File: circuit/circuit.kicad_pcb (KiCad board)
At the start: 2 copper layers, 165.5 x 103 mm, 125 parts, among them J201 Barrel_Jack, J301 Pedal5_In, J302 Guitar_In, J303 Pedal6_In, J304 Amp_Out, J305 Pedal1_In, J306 Pedal7_In, J307 Pedal2_In, J308 Pedal8_In, J309 Pedal3_In, J310 Pedal4_In, SW101 SW_Push, SW102 SW_Push, SW103 SW_Push, SW104 SW_Push, SW105 SW_Push, SW106 SW_Push, SW107 SW_Push, SW108 SW_Push, SW109 SW_Push, SW110 SW_Push, U1 AMS1117-3.3, U10 74HC595, U101 ADG419BN, U11 TL072, U12 TL072, U13 TL072, U14 TL072, U15 TL072, U16 CD4051B, U17 CD4051B, U18 CD4051B, U19 CD4051B, U2 LM7805_TO220, U20 CD4051B, U22 CD4051B, U23 CD4051B, U24 CD4051B, U25 CD4051B, U26 CD4051B, U3 TMA-1215D, U4 LM7905_TO220, U5 ESP32-S3-DevKitC, U7 74HC595, U8 74HC595, U9 74HC595

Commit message: Created pdf and made minor readabilty changes.
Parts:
- added C201: 10uF, Capacitor_THT:C_Axial_L3.8mm_D2.6mm_P7.50mm_Horizontal, F.Cu at (132.0, 46.0)
- added C202: 100uF, Capacitor_THT:C_Axial_L3.8mm_D2.6mm_P7.50mm_Horizontal, F.Cu at (132.0, 51.0)
- added C203: 0.1uF, Capacitor_THT:C_Axial_L3.8mm_D2.6mm_P7.50mm_Horizontal, F.Cu at (65.0, 30.0)
- added C204: 0.1uF, Capacitor_THT:C_Axial_L3.8mm_D2.6mm_P7.50mm_Horizontal, F.Cu at (107.0, 66.0)
- C101, C102, C103, C104, C105, C106, C107, C108, C109, C110: value 0.1mF -> .1uF
- C111, C112, C113, C114, C115, C116, C117, C118, C119, C120, C121, C122, C123, C124, C125, C126, C127, C128, C129, C130, C131, C132, C206, C208: value 0.1mF -> 0.1uF
- C205, C207: value 0.33mF -> 0.33uF
- C209, C210: value 10mF -> 10uF
- C303, C304, C305, C306, C311, C312, C313, C314, C318, C319: value 1mF -> 1uF
- moved C313 100.2 mm to (133.0, 96.0)
- moved C201 94.2 mm to (196.0, 79.5), turned to 180 degrees
- moved NT101 89.1 mm to (187.0, 117.0)
- moved C304 84.3 mm to (152.0, 117.0)
- moved R306 82.7 mm to (125.0, 94.0)
- moved U2 82.5 mm to (139.5, 121.5), turned to 180 degrees
- moved C318 82.0 mm to (121.0, 85.0)
- moved C205 80.3 mm to (137.0, 112.0)
- moved C206 76.7 mm to (143.0, 117.0), turned to 180 degrees
- moved SW110 75.2 mm to (180.0, 102.0), turned to 180 degrees
- moved C309 73.8 mm to (125.0, 60.0)
- moved C109 73.2 mm to (174.3, 96.0)
- moved U3 73.0 mm to (140.0, 57.0)
- moved R308 72.8 mm to (117.0, 70.0)
- moved C303 70.2 mm to (119.0, 90.0)
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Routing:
- net VIN_12V: track 155.3 -> 8.70 mm
- net Net-(Disp101-SDA): track 107.1 -> 28.5 mm
- net Net-(Disp101-SCL): track 105.8 -> 27.5 mm
- net 3.3V: track 70.4 -> 0.00 mm, vias 1 -> 0
- net Net-(U5-GPIO9/ADC1_CH8): track 5.15 -> 71.6 mm, vias 0 -> 2
- net Net-(D201-A): track 68.8 -> 15.1 mm
- net Net-(U5-GPIO8/ADC1_CH7): track 4.89 -> 56.7 mm
- net Net-(U5-GPIO7/ADC1_CH6): track 5.23 -> 57.0 mm
- net Net-(U5-GPIO14/ADC2_CH3): track 89.1 -> 41.0 mm
- net Net-(U1-VO): track 53.6 -> 6.30 mm
- net PEDAL_5_IN: track 45.0 -> 0.00 mm
- net /U9_Q4: track 44.1 -> 0.00 mm
- net /U9_Q6: track 43.5 -> 0.00 mm
- net /U9_Q5: track 43.5 -> 0.00 mm
- net SR_STCP: track 0.00 -> 41.7 mm
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
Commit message: Changed default pin assignments and setp sdkconfig.defaults
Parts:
- moved C113 165.6 mm to (-2.25, 108.5)
- moved C319 151.1 mm to (-16.1, 85.3)
- moved R308 140.6 mm to (-11.6, 13.2)
- moved R301 138.8 mm to (-9.12, 90.3)
- moved C318 133.9 mm to (7.38, 14.2)
- moved U10 131.9 mm to (119.5, -67.1)
- moved C313 128.5 mm to (4.88, 106.3)
- moved U18 126.2 mm to (-13.6, 22.2)
- moved C210 122.3 mm to (10.9, 111.3)
- moved R302 122.0 mm to (11.8, 94.5)
- moved R306 119.4 mm to (5.88, 102.3)
- moved C118 117.4 mm to (135.2, 9.00)
- moved C303 117.2 mm to (1.88, 94.3)
- moved U17 115.7 mm to (135.1, 15.4)
- moved C129 115.0 mm to (163.0, 120.0)
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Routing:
- net SR_OE: track 0.00 -> 216.6 mm
- net -15V: track 0.00 -> 87.2 mm
- net SR_STCP: track 41.7 -> 118.6 mm, vias 0 -> 1
- net +15V: track 0.00 -> 74.6 mm
- net Net-(U12-1+): track 0.00 -> 63.1 mm
- net SR_SHCP: track 36.1 -> 80.9 mm, vias 0 -> 1
- net SR_DS: track 32.3 -> 74.5 mm, vias 0 -> 3
- net /IO Routing/U7_Q5: track 0.00 -> 37.3 mm
- net /IO Routing/U7_Q6: track 0.00 -> 35.5 mm
- net /IO Routing/U7_Q4: track 0.00 -> 35.3 mm
- net /IO Routing/U7_Q7: track 0.00 -> 33.7 mm
- net /IO Routing/U7_Q3: track 0.00 -> 20.6 mm
- net /IO Routing/U7_Q2: track 0.00 -> 20.6 mm
- net /IO Routing/U7_Q0: track 0.00 -> 14.3 mm
- net 3.3V: track 0.00 -> 2.54 mm
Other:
- board size 165.5 x 103 mm -> 165.5 x 142.5 mm

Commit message: Very tentative PCB layout, Code compiles but needs major functionality testing.
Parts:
- removed the C201 at (196.0, 79.5)
- removed the C201 at (132.0, 45.0)
- removed the C202 at (188.8, 83.0)
- removed the C202 at (132.0, 50.0)
- removed the C203 at (52.0, 50.0)
- removed the C203 at (52.0, 45.0)
- removed the C204 at (109.0, 51.0)
- removed the C204 at (49.0, 30.0)
- added C201: 10uF, Capacitor_THT:C_Axial_L3.8mm_D2.6mm_P7.50mm_Horizontal, F.Cu at (184.5, 136.5)
- added C202: 100uF, Capacitor_THT:C_Axial_L3.8mm_D2.6mm_P7.50mm_Horizontal, F.Cu at (195.0, 137.5)
- added C203: 0.1uF, Capacitor_THT:C_Axial_L3.8mm_D2.6mm_P7.50mm_Horizontal, F.Cu at (117.0, 91.0)
- added C204: 0.1uF, Capacitor_THT:C_Axial_L3.8mm_D2.6mm_P7.50mm_Horizontal, F.Cu at (135.2, 126.5)
- added C801: 0.1uF, Capacitor_THT:C_Axial_L3.8mm_D2.6mm_P7.50mm_Horizontal, F.Cu at (170.8, 78.9)
- added C802: 0.1uF, Capacitor_THT:C_Axial_L3.8mm_D2.6mm_P7.50mm_Horizontal, F.Cu at (181.3, 79.9)
- added D100: LED_PWR, Connector_Wire:SolderWire-0.1sqmm_1x02_P3.6mm_D0.4mm_OD1mm, F.Cu at (234.9, 149.8)
- added D801: Pedal_1, Connector_Wire:SolderWire-0.1sqmm_1x02_P3.6mm_D0.4mm_OD1mm, F.Cu at (150.5, 38.8)
- added D802: Pedal_2, Connector_Wire:SolderWire-0.1sqmm_1x02_P3.6mm_D0.4mm_OD1mm, F.Cu at (156.0, 38.8)
- added D803: Pedal_3, Connector_Wire:SolderWire-0.1sqmm_1x02_P3.6mm_D0.4mm_OD1mm, F.Cu at (161.5, 38.8)
- added D804: Pedal_4, Connector_Wire:SolderWire-0.1sqmm_1x02_P3.6mm_D0.4mm_OD1mm, F.Cu at (167.0, 38.8)
- added D805: Status, Connector_Wire:SolderWire-0.1sqmm_1x02_P3.6mm_D0.4mm_OD1mm, F.Cu at (172.5, 38.5)
- added D806: Pedal_5, Connector_Wire:SolderWire-0.1sqmm_1x02_P3.6mm_D0.4mm_OD1mm, F.Cu at (178.0, 38.5)
- added D807: Pedal_6, Connector_Wire:SolderWire-0.1sqmm_1x02_P3.6mm_D0.4mm_OD1mm, F.Cu at (183.5, 38.5)
- added D808: Pedal_7, Connector_Wire:SolderWire-0.1sqmm_1x02_P3.6mm_D0.4mm_OD1mm, F.Cu at (189.0, 38.3)
- added D809: Pedal_8, Connector_Wire:SolderWire-0.1sqmm_1x02_P3.6mm_D0.4mm_OD1mm, F.Cu at (194.5, 38.3)
- added R101: 100, Resistor_THT:R_Axial_DIN0204_L3.6mm_D1.6mm_P5.08mm_Horizontal, F.Cu at (229.4, 145.3)
- added R801: 150, Resistor_THT:R_Axial_DIN0204_L3.6mm_D1.6mm_P5.08mm_Horizontal, F.Cu at (147.6, 43.4)
- added R802: 150, Resistor_THT:R_Axial_DIN0204_L3.6mm_D1.6mm_P5.08mm_Horizontal, F.Cu at (153.8, 46.2)
- added R803: 150, Resistor_THT:R_Axial_DIN0204_L3.6mm_D1.6mm_P5.08mm_Horizontal, F.Cu at (160.1, 43.4)
- added R804: 150, Resistor_THT:R_Axial_DIN0204_L3.6mm_D1.6mm_P5.08mm_Horizontal, F.Cu at (166.4, 46.2)
- added R805: 150, Resistor_THT:R_Axial_DIN0204_L3.6mm_D1.6mm_P5.08mm_Horizontal, F.Cu at (172.7, 43.4)
- added R806: 150, Resistor_THT:R_Axial_DIN0204_L3.6mm_D1.6mm_P5.08mm_Horizontal, F.Cu at (178.9, 46.2)
- added R807: 150, Resistor_THT:R_Axial_DIN0204_L3.6mm_D1.6mm_P5.08mm_Horizontal, F.Cu at (232.4, 95.8)
- added R808: 150, Resistor_THT:R_Axial_DIN0204_L3.6mm_D1.6mm_P5.08mm_Horizontal, F.Cu at (185.3, 43.4)
- added R809: 150, Resistor_THT:R_Axial_DIN0204_L3.6mm_D1.6mm_P5.08mm_Horizontal, F.Cu at (191.5, 46.2)
- added RV101: 500, Potentiometer_THT:Potentiometer_Bourns_3339P_Vertical, F.Cu at (223.5, 147.8)
- added U801: 74HC595, Package_DIP:CERDIP-16_W7.62mm_SideBrazed, F.Cu at (163.4, 55.1)
- added U802: 74HC595, Package_DIP:CERDIP-16_W7.62mm_SideBrazed, F.Cu at (173.7, 56.1)
- C101, C102, C103, C104, C105, C106, C107, C108, C109, C110, C701, C702, C703, C704: value .1uF -> 0.1uF
- Disp101: footprint Connector_JST:JST_EH_B4B-EH-A_1x04_P2.50mm_Vertical -> Connector_PinHeader_1.00mm:PinHeader_1x04_P1.00mm_Vertical
- J301, J302, J303, J304, J305, J306, J307, J308, J309, J310: footprint Connector_Wire:SolderWire-0.1sqmm_1x02_P3.6mm_D0.4mm_OD1mm -> Bay:Pedal_Jack
- SW101: value SW_Push -> Pedal_1
- SW102: value SW_Push -> Pedal_2
- SW103: value SW_Push -> Pedal_3
- SW104: value SW_Push -> Pedal_4
- SW105: value SW_Push -> Pedal_5
- SW106: value SW_Push -> Pedal_6
- SW107: value SW_Push -> Pedal_7
- SW108: value SW_Push -> Pedal_8
- SW109: value SW_Push -> Program
- SW110: value SW_Push -> Preset
- moved C318 254.6 mm to (229.4, 138.8)
- moved R309 240.0 mm to (203.4, 123.8)
- moved C319 224.8 mm to (203.4, 133.8)
- moved C303 220.4 mm to (218.4, 135.8)
- moved C210 217.5 mm to (226.4, 140.8)
- moved R304 213.9 mm to (222.4, 92.8)
- moved C311 212.7 mm to (221.4, 96.8)
- moved R308 199.3 mm to (153.4, 125.0)
- moved C313 171.4 mm to (175.4, 123.8)
- moved R302 171.3 mm to (179.4, 129.8)
- moved R301 158.4 mm to (145.0, 127.0)
- moved R306 149.7 mm to (155.0, 89.0)
- moved C127 144.3 mm to (140.0, 79.3), turned to 180 degrees
- moved C131 138.3 mm to (129.7, 79.2), turned to 180 degrees
- moved C126 133.4 mm to (142.8, 49.1)
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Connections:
- net /Pedal Routing 1 - 4/U8_Q0 renamed /Matrix Shift Registers/U8_Q0
- net /Pedal Routing 1 - 4/U8_Q1 renamed /Matrix Shift Registers/U8_Q1
- net /Pedal Routing 1 - 4/U8_Q2 renamed /Matrix Shift Registers/U8_Q2
- net /Pedal Routing 1 - 4/U8_Q3 renamed /Matrix Shift Registers/U8_Q3
- net /Pedal Routing 1 - 4/U8_Q4 renamed /Matrix Shift Registers/U8_Q4
- net /Pedal Routing 1 - 4/U8_Q5 renamed /Matrix Shift Registers/U8_Q5
- net /Pedal Routing 1 - 4/U8_Q6 renamed /Matrix Shift Registers/U8_Q6
- net /Pedal Routing 1 - 4/U8_Q7 renamed /Matrix Shift Registers/U8_Q7
- net SR_DS renamed MATRIX_SR_DS
- U5 pad 27: unconnected-(U5-GPIO21-Pad27) -> LED_SR_DS
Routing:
- net AGND: track 0.00 -> 761.7 mm
- net GND: track 0.00 -> 618.4 mm, vias 0 -> 3
- net 3.3V: track 2.54 -> 424.9 mm, vias 0 -> 1
- net +5V: track 3.88 -> 352.8 mm, vias 0 -> 1
- net -5V: track 0.00 -> 294.6 mm
- net ROW_6: track 0.00 -> 206.8 mm, vias 0 -> 2
- net ROW_1: track 0.00 -> 184.6 mm, vias 0 -> 5
- net ROW_3: track 0.00 -> 174.4 mm, vias 0 -> 2
- net ROW_4: track 0.00 -> 166.4 mm, vias 0 -> 2
- net ROW_5: track 0.00 -> 161.1 mm
- net ROW_2: track 0.00 -> 158.2 mm
- net ROW_7: track 0.00 -> 157.1 mm
- net Net-(C314-Pad1): track 0.00 -> 137.3 mm
- net SR_SHCP: track 80.9 -> 216.2 mm, vias 1 -> 5
- net ROW_9: track 0.00 -> 133.7 mm, vias 0 -> 1
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- removed copper zone on B.Cu, net AGND
- removed copper zone on B.Cu, net GND
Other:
- board size 165.5 x 142.5 mm -> 183.2 x 119.6 mm

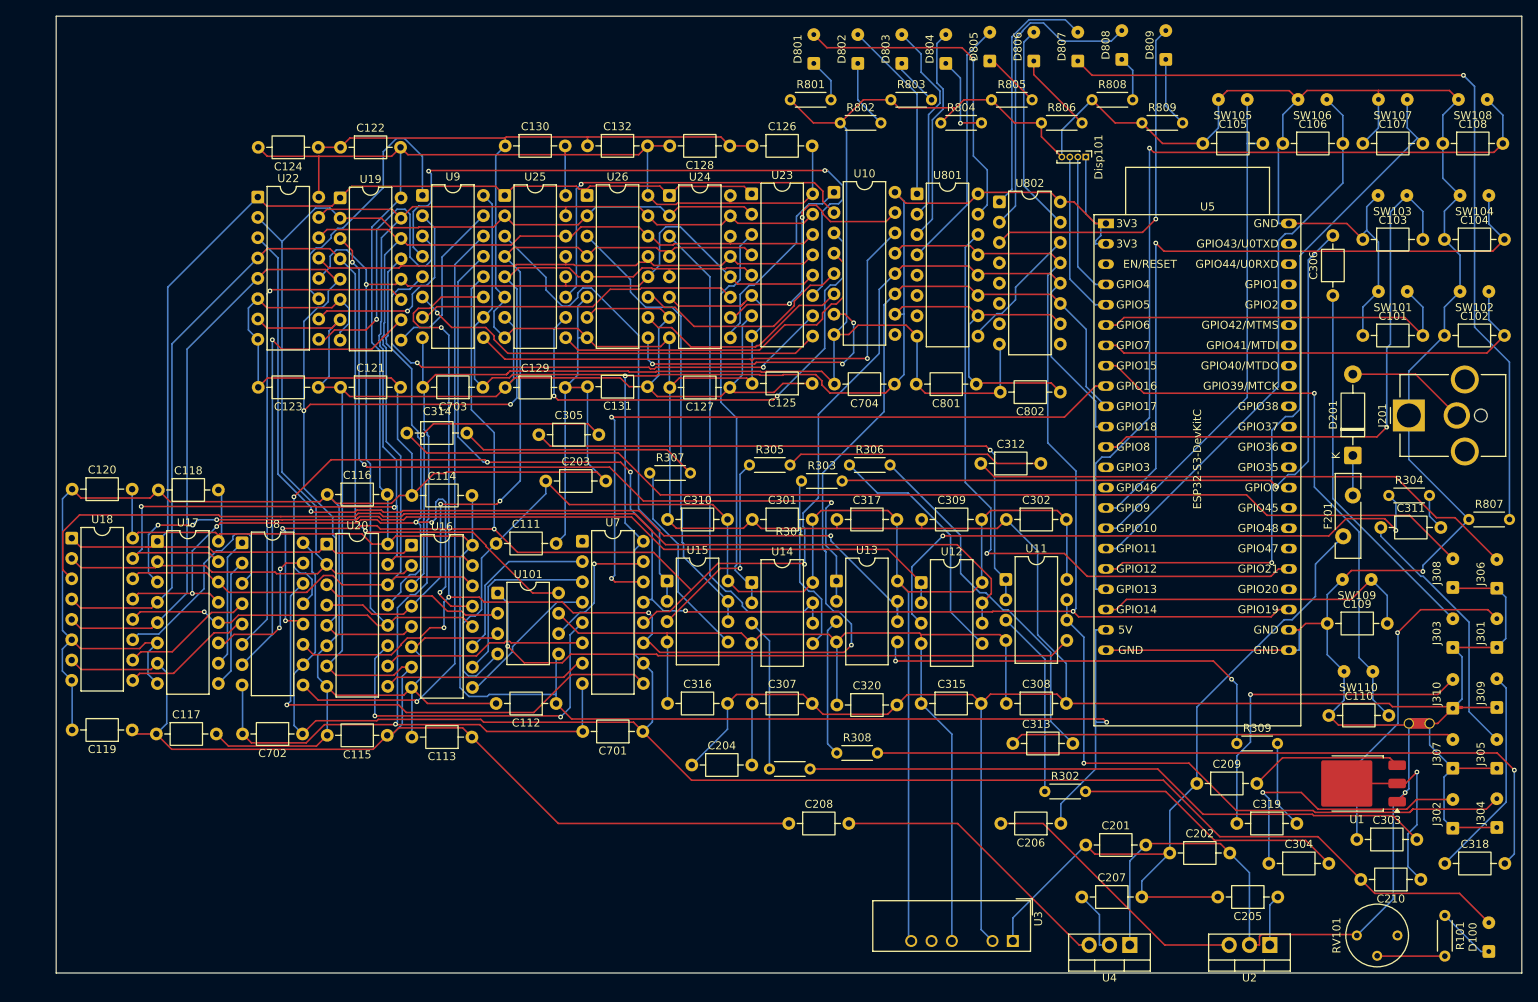
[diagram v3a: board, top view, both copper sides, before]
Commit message: Re-annotation of circuit, new PCB routing, updated PDF
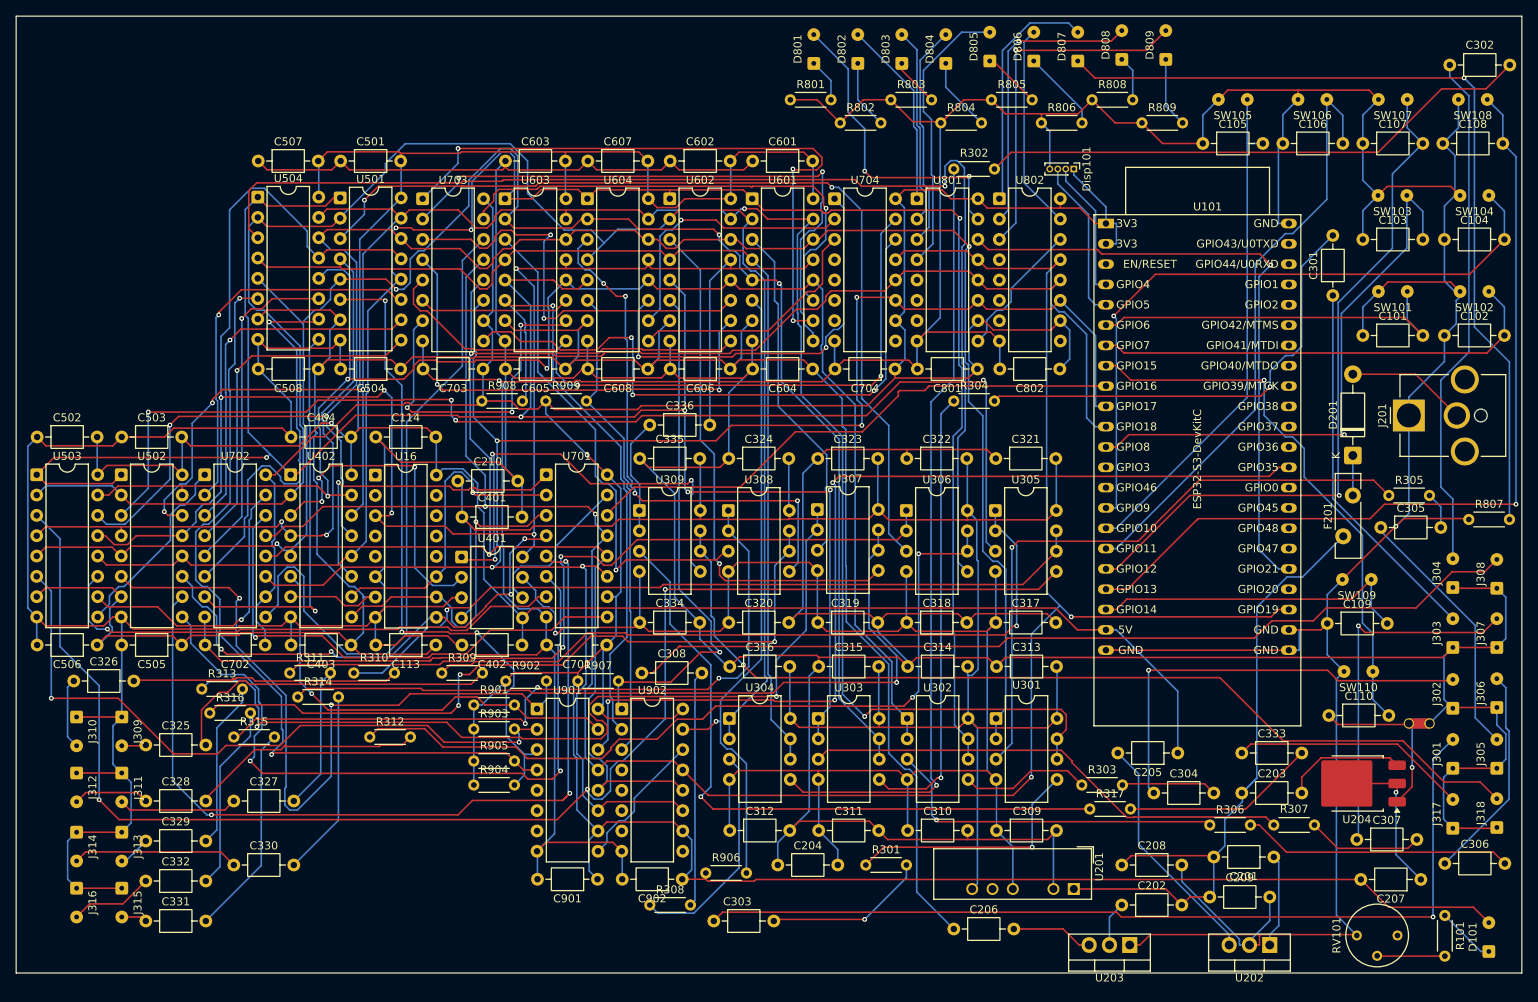
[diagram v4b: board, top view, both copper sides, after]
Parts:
- added C317: 0.1uF, Capacitor_THT:C_Axial_L3.8mm_D2.6mm_P7.50mm_Horizontal, F.Cu at (173.2, 108.7)
- added C318: 0.1uF, Capacitor_THT:C_Axial_L3.8mm_D2.6mm_P7.50mm_Horizontal, F.Cu at (162.1, 108.7)
- added C319: 0.1uF, Capacitor_THT:C_Axial_L3.8mm_D2.6mm_P7.50mm_Horizontal, F.Cu at (151.0, 108.7)
- added C320: 0.1uF, Capacitor_THT:C_Axial_L3.8mm_D2.6mm_P7.50mm_Horizontal, F.Cu at (139.9, 108.7)
- added C321: 0.1uF, Capacitor_THT:C_Axial_L3.8mm_D2.6mm_P7.50mm_Horizontal, F.Cu at (173.2, 88.2)
- added C322: 0.1uF, Capacitor_THT:C_Axial_L3.8mm_D2.6mm_P7.50mm_Horizontal, F.Cu at (162.1, 88.2)
- added C323: 0.1uF, Capacitor_THT:C_Axial_L3.8mm_D2.6mm_P7.50mm_Horizontal, F.Cu at (151.0, 88.2)
- added C324: 0.1uF, Capacitor_THT:C_Axial_L3.8mm_D2.6mm_P7.50mm_Horizontal, F.Cu at (139.9, 88.2)
- added C325: 1uF, Capacitor_THT:C_Axial_L3.8mm_D2.6mm_P7.50mm_Horizontal, F.Cu at (67.0, 124.0)
- added C326: 1uF, Capacitor_THT:C_Axial_L3.8mm_D2.6mm_P7.50mm_Horizontal, F.Cu at (58.0, 116.0)
- added C327: 1uF, Capacitor_THT:C_Axial_L3.8mm_D2.6mm_P7.50mm_Horizontal, F.Cu at (78.0, 131.0)
- added C328: 1uF, Capacitor_THT:C_Axial_L3.8mm_D2.6mm_P7.50mm_Horizontal, F.Cu at (67.0, 131.0)
- added C329: 1uF, Capacitor_THT:C_Axial_L3.8mm_D2.6mm_P7.50mm_Horizontal, F.Cu at (67.0, 136.0)
- added C330: 1uF, Capacitor_THT:C_Axial_L3.8mm_D2.6mm_P7.50mm_Horizontal, F.Cu at (78.0, 139.0)
- added C331: 1uF, Capacitor_THT:C_Axial_L3.8mm_D2.6mm_P7.50mm_Horizontal, F.Cu at (67.0, 146.0)
- added C332: 1uF, Capacitor_THT:C_Axial_L3.8mm_D2.6mm_P7.50mm_Horizontal, F.Cu at (67.0, 141.0)
- added C901: 0.1uF, Capacitor_THT:C_Axial_L3.8mm_D2.6mm_P7.50mm_Horizontal, F.Cu at (123.5, 140.8)
- added C902: 0.1uF, Capacitor_THT:C_Axial_L3.8mm_D2.6mm_P7.50mm_Horizontal, F.Cu at (134.1, 140.8)
- added J309: FX_S_1, Bay:Pedal_Jack, F.Cu at (64.0, 120.5)
- added J310: FX_S_2, Bay:Pedal_Jack, F.Cu at (58.4, 120.5)
- added J311: FX_S_3, Bay:Pedal_Jack, F.Cu at (64.0, 127.5)
- added J312: FX_S_4, Bay:Pedal_Jack, F.Cu at (58.4, 127.5)
- added J313: FX_S_5, Bay:Pedal_Jack, F.Cu at (64.0, 134.9)
- added J314: FX_S_6, Bay:Pedal_Jack, F.Cu at (58.4, 134.9)
- added J315: FX_S_7, Bay:Pedal_Jack, F.Cu at (64.0, 141.9)
- added J316: FX_S_8, Bay:Pedal_Jack, F.Cu at (58.4, 141.9)
- added R309: 10k, Resistor_THT:R_Axial_DIN0204_L3.6mm_D1.6mm_P5.08mm_Horizontal, F.Cu at (104.0, 115.0)
- added R310: 10k, Resistor_THT:R_Axial_DIN0204_L3.6mm_D1.6mm_P5.08mm_Horizontal, F.Cu at (93.0, 115.0)
- added R311: 10k, Resistor_THT:R_Axial_DIN0204_L3.6mm_D1.6mm_P5.08mm_Horizontal, F.Cu at (85.0, 115.0)
- added R312: 10k, Resistor_THT:R_Axial_DIN0204_L3.6mm_D1.6mm_P5.08mm_Horizontal, F.Cu at (95.0, 123.0)
- added R313: 10k, Resistor_THT:R_Axial_DIN0204_L3.6mm_D1.6mm_P5.08mm_Horizontal, F.Cu at (74.0, 117.0)
- added R314: 10k, Resistor_THT:R_Axial_DIN0204_L3.6mm_D1.6mm_P5.08mm_Horizontal, F.Cu at (86.0, 118.0)
- added R315: 10k, Resistor_THT:R_Axial_DIN0204_L3.6mm_D1.6mm_P5.08mm_Horizontal, F.Cu at (78.0, 123.0)
- added R316: 10k, Resistor_THT:R_Axial_DIN0204_L3.6mm_D1.6mm_P5.08mm_Horizontal, F.Cu at (75.0, 120.0)
- added R901: 10k, Resistor_THT:R_Axial_DIN0204_L3.6mm_D1.6mm_P5.08mm_Horizontal, F.Cu at (108.0, 119.0)
- added R902: 10k, Resistor_THT:R_Axial_DIN0204_L3.6mm_D1.6mm_P5.08mm_Horizontal, F.Cu at (112.0, 116.0)
- added R903: 10k, Resistor_THT:R_Axial_DIN0204_L3.6mm_D1.6mm_P5.08mm_Horizontal, F.Cu at (108.0, 122.0)
- added R904: 10k, Resistor_THT:R_Axial_DIN0204_L3.6mm_D1.6mm_P5.08mm_Horizontal, F.Cu at (108.0, 129.0)
- added R905: 10k, Resistor_THT:R_Axial_DIN0204_L3.6mm_D1.6mm_P5.08mm_Horizontal, F.Cu at (108.0, 126.0)
- added R906: 10k, Resistor_THT:R_Axial_DIN0204_L3.6mm_D1.6mm_P5.08mm_Horizontal, F.Cu at (137.0, 140.0)
- added R907: 10k, Resistor_THT:R_Axial_DIN0204_L3.6mm_D1.6mm_P5.08mm_Horizontal, F.Cu at (121.0, 116.0)
- added R908: 10k, Resistor_THT:R_Axial_DIN0204_L3.6mm_D1.6mm_P5.08mm_Horizontal, F.Cu at (109.0, 81.0)
- added R909: 10k, Resistor_THT:R_Axial_DIN0204_L3.6mm_D1.6mm_P5.08mm_Horizontal, F.Cu at (117.0, 81.0)
- added U305: TL072, Package_DIP:CERDIP-8_W7.62mm_SideBrazed, F.Cu at (173.2, 94.7)
- added U306: TL072, Package_DIP:CERDIP-8_W7.62mm_SideBrazed, F.Cu at (162.1, 94.7)
- added U307: TL072, Package_DIP:CERDIP-8_W7.62mm_SideBrazed, F.Cu at (150.9, 94.6)
- added U308: TL072, Package_DIP:CERDIP-8_W7.62mm_SideBrazed, F.Cu at (139.8, 94.7)
- added U901: 74HC595, Package_DIP:CERDIP-16_W7.62mm_SideBrazed, F.Cu at (115.9, 119.5)
- added U902: 74HC595, Package_DIP:CERDIP-16_W7.62mm_SideBrazed, F.Cu at (126.5, 119.5)
- J301: renamed from J307; value Pedal2_In -> FX_R_2
- J302: renamed from J310; value Pedal4_In -> FX_R_4
- J303: value Pedal6_In -> FX_R_56
- J304: renamed from J308; value Pedal8_In -> FX_R_8
- J305: value Pedal1_In -> FX_R_1
- J306: renamed from J309; value Pedal3_In -> FX_R_3
- J307: renamed from J301; value Pedal5_In -> FX_R_5
- J308: renamed from J306; value Pedal7_In -> FX_R_7
- moved C302 138.2 mm to (230.0, 39.0)
- moved R307 63.4 mm to (208.0, 134.0)
- moved R308 56.4 mm to (130.0, 144.0)
- moved R302 53.7 mm to (168.0, 52.0)
- moved R301 50.0 mm to (157.0, 139.0)
- moved C308 49.8 mm to (129.0, 115.0)
- moved R306 47.5 mm to (200.0, 134.0)
- moved C334 46.9 mm to (128.8, 108.7)
- moved U309 46.6 mm to (128.7, 94.7)
- moved C335 46.4 mm to (128.8, 88.2)
- moved C303 43.5 mm to (138.0, 146.0)
- moved C206 24.5 mm to (168.0, 147.0)
- moved R304 21.5 mm to (168.0, 81.0)
- moved C313 20.6 mm to (173.3, 114.2)
- moved C314 20.4 mm to (162.2, 114.2)
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- renumbered C205 to C201, C207 to C202, C209 to C203, C206 to C205, C208 to C206, C210 to C207, C201 to C208, C202 to C209, C203 to C210, C306 to C301, C314 to C302, C313 to C303, C319 to C304, C311 to C305, C318 to C306, C303 to C307, C312 to C308, C315 to C309, C320 to C310, C307 to C311, C316 to C312, C309 to C313, C317 to C314, C301 to C315, C310 to C316, C304 to C333, C308 to C334, C302 to C335, C305 to C336, C111 to C401, C112 to C402, C115 to C403, C116 to C404, C122 to C501, C120 to C502, C118 to C503, C121 to C504, C117 to C505, C119 to C506, C124 to C507, C123 to C508, C126 to C601, C128 to C602, C130 to C603, C125 to C604, C129 to C605, C127 to C606, C132 to C607, C131 to C608, D100 to D101, J302 to J317, J304 to J318, R306 to R301, R307 to R302, R309 to R303, R303 to R304, R304 to R305, R308 to R306, R301 to R307, R305 to R308, R302 to R317, U5 to U101, U3 to U201, U2 to U202, U4 to U203, U1 to U204, U12 to U301, U13 to U302, U14 to U303, U15 to U304, U11 to U309, U101 to U401, U20 to U402, U19 to U501, U17 to U502, U18 to U503, U22 to U504, U23 to U601, U24 to U602, U25 to U603, U26 to U604, U7 to U701, U8 to U702, U9 to U703, U10 to U704
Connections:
- U101 pad 32: unconnected-(U5-GPIO35-Pad32) -> INHIBIT_SR_DS
- U301 pad 1: PEDAL_1_IN -> FX_R_1
- U301 pad 2: PEDAL_1_IN -> FX_R_1
- U301 pad 6: PEDAL_2_IN -> FX_R_2
- U301 pad 7: PEDAL_2_IN -> FX_R_2
- U302 pad 1: PEDAL_3_IN -> FX_R_3
- U302 pad 2: PEDAL_3_IN -> FX_R_3
- U302 pad 6: PEDAL_4_IN -> FX_R_4
- U302 pad 7: PEDAL_4_IN -> FX_R_4
- U303 pad 1: PEDAL_5_IN -> FX_R_5
- U303 pad 2: PEDAL_5_IN -> FX_R_5
- U303 pad 6: PEDAL_6_IN -> FX_R_6
- U303 pad 7: PEDAL_6_IN -> FX_R_6
- U304 pad 1: PEDAL_7_IN -> FX_R_7
- U304 pad 2: PEDAL_7_IN -> FX_R_7
- U304 pad 6: PEDAL_8_IN -> FX_R_8
- U304 pad 7: PEDAL_8_IN -> FX_R_8
- U401 pad 8: ROW_9 -> GUITAR_IN
- U402 pad 1: ROW_5 -> FX_R_5
- U402 pad 10: /IO Routing/U7_Q6 -> /IO Routing/U7_Q2
- U402 pad 11: /IO Routing/U7_Q5 -> /IO Routing/U7_Q1
- U402 pad 12: ROW_4 -> FX_R_4
- U402 pad 13: ROW_1 -> FX_R_1
- U402 pad 14: ROW_2 -> FX_R_2
- U402 pad 15: ROW_3 -> FX_R_3
- U402 pad 2: ROW_7 -> FX_R_7
- U402 pad 4: ROW_8 -> FX_R_8
- U402 pad 5: ROW_6 -> FX_R_6
- U402 pad 6: AGND -> /IO Routing/U901_Q0
- U402 pad 9: /IO Routing/U7_Q7 -> /IO Routing/U7_Q3
- U501 pad 1: ROW_5 -> FX_R_5
- U501 pad 10: /Matrix Shift Registers/U8_Q7 -> /Matrix Shift Registers/U8_Q3
- U501 pad 11: /Matrix Shift Registers/U8_Q6 -> /Matrix Shift Registers/U8_Q2
- U501 pad 12: ROW_4 -> FX_R_4
- U501 pad 13: ROW_1 -> GUITAR_IN
- U501 pad 14: ROW_2 -> FX_R_1
- U501 pad 15: ROW_3 -> FX_R_2
- U501 pad 2: ROW_7 -> FX_R_7
- U501 pad 3: PEDAL_3_IN -> FX_S_3
- U501 pad 4: ROW_9 -> FX_R_8
- U501 pad 5: ROW_6 -> FX_R_6
- U501 pad 6: AGND -> /IO Routing/U901_Q3
- U501 pad 9: /U9_Q0 -> /Matrix Shift Registers/U8_Q4
- U502 pad 1: ROW_5 -> FX_R_5
- U502 pad 10: /Matrix Shift Registers/U8_Q1 -> /IO Routing/U7_Q5
- U502 pad 11: /Matrix Shift Registers/U8_Q0 -> /IO Routing/U7_Q4
- U502 pad 12: ROW_4 -> FX_R_4
- U502 pad 13: ROW_1 -> GUITAR_IN
- U502 pad 14: ROW_2 -> FX_R_2
- U502 pad 15: ROW_3 -> FX_R_3
- U502 pad 2: ROW_7 -> FX_R_7
- U502 pad 3: PEDAL_1_IN -> FX_S_1
- U502 pad 4: ROW_9 -> FX_R_8
- U502 pad 5: ROW_6 -> FX_R_6
- U502 pad 6: AGND -> /IO Routing/U901_Q1
- U502 pad 9: /Matrix Shift Registers/U8_Q2 -> /IO Routing/U7_Q6
- U503 pad 1: ROW_5 -> FX_R_5
- U503 pad 10: /Matrix Shift Registers/U8_Q4 -> /Matrix Shift Registers/U8_Q0
- U503 pad 11: /Matrix Shift Registers/U8_Q3 -> /IO Routing/U7_Q7
- U503 pad 12: ROW_4 -> FX_R_4
- U503 pad 13: ROW_1 -> GUITAR_IN
- U503 pad 14: ROW_2 -> FX_R_1
- U503 pad 15: ROW_3 -> FX_R_3
- U503 pad 2: ROW_7 -> FX_R_7
- U503 pad 3: PEDAL_2_IN -> FX_S_2
- U503 pad 4: ROW_9 -> FX_R_8
- U503 pad 5: ROW_6 -> FX_R_6
- U503 pad 6: AGND -> /IO Routing/U901_Q2
- U503 pad 9: /Matrix Shift Registers/U8_Q5 -> /Matrix Shift Registers/U8_Q1
- U504 pad 1: ROW_5 -> FX_R_5
- U504 pad 10: /U9_Q2 -> /Matrix Shift Registers/U8_Q6
- U504 pad 11: /U9_Q1 -> /Matrix Shift Registers/U8_Q5
- U504 pad 12: ROW_4 -> FX_R_3
- U504 pad 13: ROW_1 -> GUITAR_IN
- U504 pad 14: ROW_2 -> FX_R_1
- U504 pad 15: ROW_3 -> FX_R_2
- U504 pad 2: ROW_7 -> FX_R_7
- U504 pad 3: PEDAL_4_IN -> FX_S_4
- U504 pad 4: ROW_9 -> FX_R_8
- U504 pad 5: ROW_6 -> FX_R_6
- U504 pad 6: AGND -> /IO Routing/U901_Q4
- U504 pad 9: /U9_Q3 -> /Matrix Shift Registers/U8_Q7
- U601 pad 1: ROW_5 -> FX_R_4
- U601 pad 10: /U9_Q5 -> /Matrix Shift Registers/U9_Q1
- U601 pad 11: /U9_Q4 -> /Matrix Shift Registers/U9_Q0
- U601 pad 12: ROW_4 -> FX_R_3
- U601 pad 13: ROW_1 -> GUITAR_IN
- U601 pad 14: ROW_2 -> FX_R_1
- U601 pad 15: ROW_3 -> FX_R_2
- U601 pad 2: ROW_7 -> FX_R_7
- U601 pad 3: PEDAL_5_IN -> FX_S_5
- U601 pad 4: ROW_8 -> FX_R_8
- U601 pad 5: ROW_6 -> FX_R_6
- U601 pad 6: AGND -> /Inhibit Registers/U902_Q0
- U601 pad 9: /U9_Q6 -> /Matrix Shift Registers/U9_Q2
- U602 pad 1: ROW_5 -> FX_R_4
- U602 pad 10: /U10_Q0 -> /Matrix Shift Registers/U9_Q4
- U602 pad 11: /U9_Q7 -> /Matrix Shift Registers/U9_Q3
- U602 pad 12: ROW_4 -> FX_R_3
- U602 pad 13: ROW_1 -> GUITAR_IN
- U602 pad 14: ROW_2 -> FX_R_1
- U602 pad 15: ROW_3 -> FX_R_2
- U602 pad 2: ROW_7 -> FX_R_7
- U602 pad 3: PEDAL_6_IN -> FX_S_6
- U602 pad 4: ROW_8 -> FX_R_8
- U602 pad 5: ROW_6 -> FX_R_5
- U602 pad 6: AGND -> /Inhibit Registers/U902_Q1
- U602 pad 9: /U10_Q1 -> /Matrix Shift Registers/U9_Q5
- U603 pad 1: ROW_5 -> FX_R_4
- U603 pad 10: /U10_Q3 -> /Matrix Shift Registers/U9_Q7
- U603 pad 11: /U10_Q2 -> /Matrix Shift Registers/U9_Q6
- U603 pad 12: ROW_4 -> FX_R_3
- U603 pad 13: ROW_1 -> GUITAR_IN
- U603 pad 14: ROW_2 -> FX_R_1
- U603 pad 15: ROW_3 -> FX_R_2
- U603 pad 2: ROW_7 -> FX_R_6
- U603 pad 3: PEDAL_7_IN -> FX_S_7
- U603 pad 4: ROW_8 -> FX_R_8
- U603 pad 5: ROW_6 -> FX_R_5
- U603 pad 6: AGND -> /Inhibit Registers/U902_Q2
- U603 pad 9: /U10_Q4 -> /Matrix Shift Registers/U10_Q0
- U604 pad 1: ROW_5 -> FX_R_4
- U604 pad 10: /U10_Q6 -> /Matrix Shift Registers/U10_Q2
- U604 pad 11: /U10_Q5 -> /Matrix Shift Registers/U10_Q1
- U604 pad 12: ROW_4 -> FX_R_3
- U604 pad 13: ROW_1 -> GUITAR_IN
- U604 pad 14: ROW_2 -> FX_R_1
- U604 pad 15: ROW_3 -> FX_R_2
- U604 pad 2: ROW_7 -> FX_R_6
- U604 pad 3: PEDAL_8_IN -> FX_S_8
- U604 pad 4: ROW_8 -> FX_R_7
- U604 pad 5: ROW_6 -> FX_R_5
- U604 pad 6: AGND -> /Inhibit Registers/U902_Q3
- U604 pad 9: /U10_Q7 -> /Matrix Shift Registers/U10_Q3
- U701 pad 1: unconnected-(U7-QB-Pad1) -> /IO Routing/U7_Q1
- U703 pad 1: /U9_Q1 -> /Matrix Shift Registers/U9_Q1
- U703 pad 15: /U9_Q0 -> /Matrix Shift Registers/U9_Q0
- U703 pad 2: /U9_Q2 -> /Matrix Shift Registers/U9_Q2
- U703 pad 3: /U9_Q3 -> /Matrix Shift Registers/U9_Q3
- U703 pad 4: /U9_Q4 -> /Matrix Shift Registers/U9_Q4
- U703 pad 5: /U9_Q5 -> /Matrix Shift Registers/U9_Q5
- U703 pad 6: /U9_Q6 -> /Matrix Shift Registers/U9_Q6
- U703 pad 7: /U9_Q7 -> /Matrix Shift Registers/U9_Q7
- U704 pad 1: /U10_Q1 -> /Matrix Shift Registers/U10_Q1
- U704 pad 15: /U10_Q0 -> /Matrix Shift Registers/U10_Q0
- U704 pad 2: /U10_Q2 -> /Matrix Shift Registers/U10_Q2
- U704 pad 3: /U10_Q3 -> /Matrix Shift Registers/U10_Q3
- U704 pad 4: /U10_Q4 -> unconnected-(U704-QE-Pad4)
- U704 pad 5: /U10_Q5 -> unconnected-(U704-QF-Pad5)
- U704 pad 6: /U10_Q6 -> unconnected-(U704-QG-Pad6)
- U704 pad 7: /U10_Q7 -> unconnected-(U704-QH-Pad7)
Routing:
- net FX_R_5: track 0.00 -> 250.7 mm, vias 0 -> 5
- net FX_R_2: track 0.00 -> 246.0 mm, vias 0 -> 5
- net FX_R_4: track 0.00 -> 236.7 mm, vias 0 -> 3
- net FX_R_1: track 0.00 -> 236.2 mm, vias 0 -> 3
- net FX_R_6: track 0.00 -> 226.5 mm, vias 0 -> 4
- net FX_R_7: track 0.00 -> 221.8 mm
- net FX_R_8: track 0.00 -> 210.2 mm, vias 0 -> 2
- net ROW_6: track 206.8 -> 0.00 mm, vias 2 -> 0
- net FX_R_3: track 0.00 -> 203.0 mm, vias 0 -> 3
- net GUITAR_IN: track 42.8 -> 242.9 mm, vias 1 -> 5
- net FX_S_2: track 0.00 -> 184.6 mm, vias 0 -> 3
- net ROW_1: track 184.6 -> 0.00 mm, vias 5 -> 0
- net ROW_3: track 174.4 -> 0.00 mm, vias 2 -> 0
- net ROW_4: track 166.4 -> 0.00 mm, vias 2 -> 0
- net ROW_5: track 161.1 -> 0.00 mm
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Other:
- board size 183.2 x 119.6 mm -> 188.2 x 119.6 mm
